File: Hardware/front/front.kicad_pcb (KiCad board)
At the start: 4 copper layers, 75 x 60 mm, 27 parts, among them J101 Conn_02x10_Odd_Even, SW101 Alps EC11E, SW102 C&K-D6R-Illuminated, SW103 B3W-9002-Y1C, SW104 B3W-9002-Y1C, SW105 B3W-9002-Y1C, SW106 B3W-9002-Y1C, SW107 B3W-9000-RHG2C, U101 XRA1203, U102 AT24CS32-SSHM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

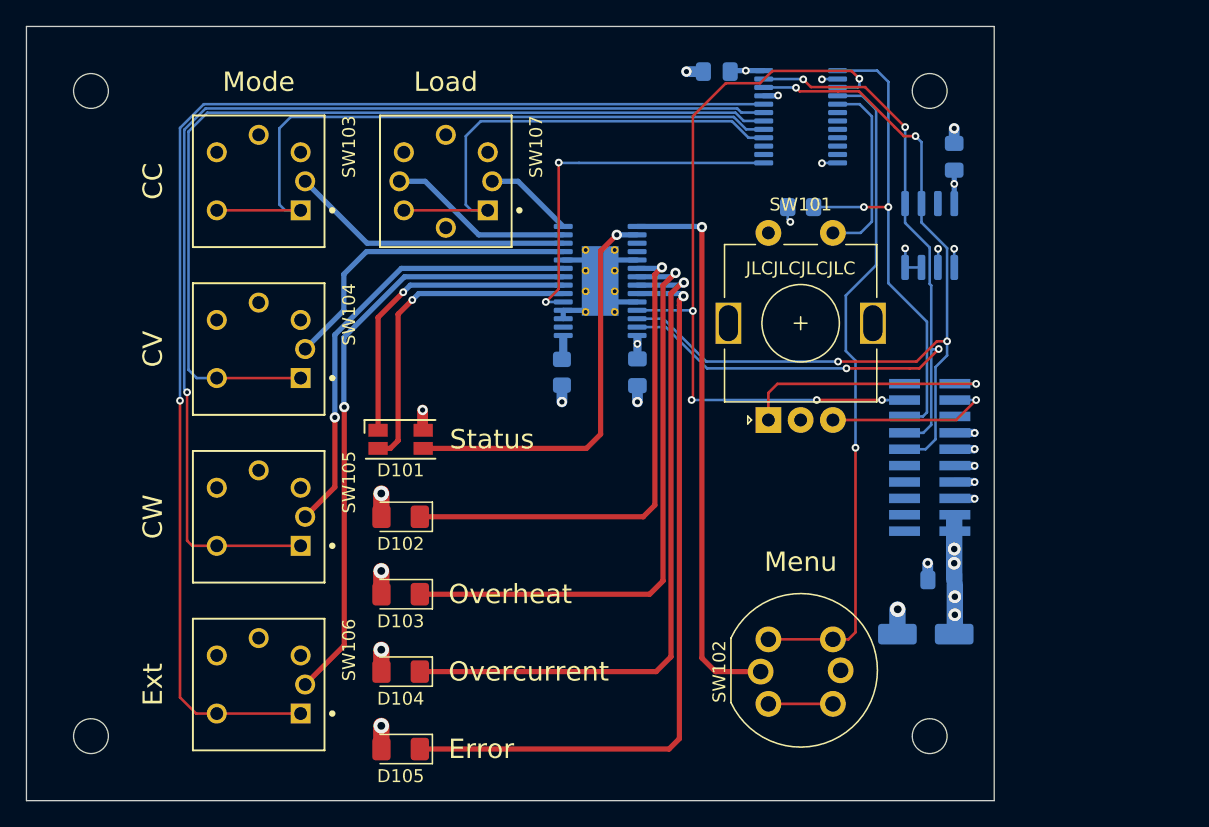
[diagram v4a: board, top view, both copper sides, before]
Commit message: Rev 2 for front panel
- Adds debouncing for all switches on the board itself, and fixes the
  incorrect RGB LED footprint.

- Fix Omron B3W-9XXX switch footprints (they had soldermask over copper)
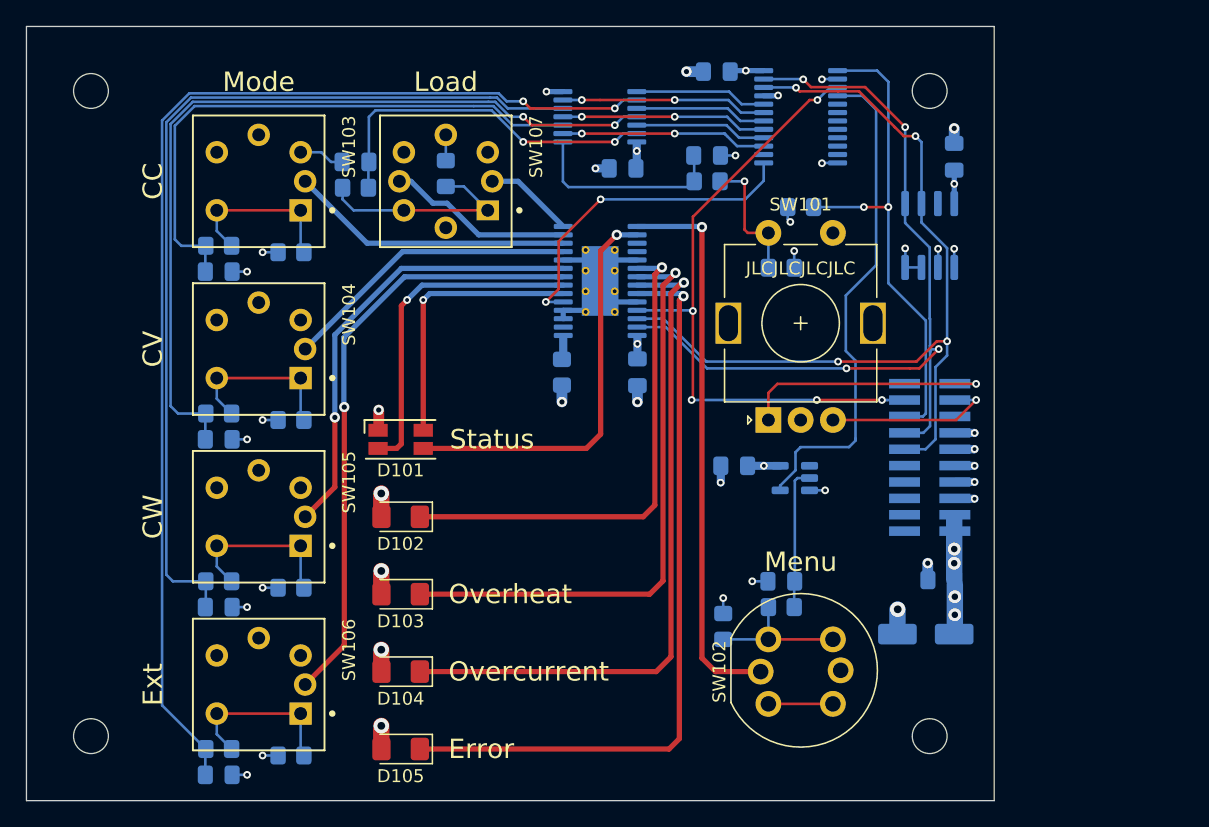
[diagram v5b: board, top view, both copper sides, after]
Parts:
- added C103: 100nF, Capacitor_SMD:C_0805_2012Metric_Pad1.18x1.45mm_HandSolder, B.Cu at (61.2, 31.0)
- added C107: 4.7µF, Capacitor_SMD:C_0805_2012Metric_Pad1.18x1.45mm_HandSolder, B.Cu at (29.9, 39.0)
- added C108: 4.7µF, Capacitor_SMD:C_0805_2012Metric_Pad1.18x1.45mm_HandSolder, B.Cu at (29.9, 52.0)
- added C109: 4.7µF, Capacitor_SMD:C_0805_2012Metric_Pad1.18x1.45mm_HandSolder, B.Cu at (29.9, 65.0)
- added C110: 4.7µF, Capacitor_SMD:C_0805_2012Metric_Pad1.18x1.45mm_HandSolder, B.Cu at (29.9, 78.0)
- added C111: 4.7µF, Capacitor_SMD:C_0805_2012Metric_Pad1.18x1.45mm_HandSolder, B.Cu at (40.5, 30.5)
- added C112: 4.7µF, Capacitor_SMD:C_0805_2012Metric_Pad1.18x1.45mm_HandSolder, B.Cu at (67.8, 30.0)
- added C113: 4.7µF, Capacitor_SMD:C_0805_2012Metric_Pad1.18x1.45mm_HandSolder, B.Cu at (73.5, 63.0)
- added C114: 100nF, Capacitor_SMD:C_0805_2012Metric_Pad1.18x1.45mm_HandSolder, B.Cu at (69.8, 54.0)
- added G***: LOGO, LOGO, B.Cu at (59.0, 71.4)
- added R103: 10k, Resistor_SMD:R_0805_2012Metric_Pad1.20x1.40mm_HandSolder, B.Cu at (35.5, 37.5)
- added R104: 10k, Resistor_SMD:R_0805_2012Metric_Pad1.20x1.40mm_HandSolder, B.Cu at (35.5, 50.5)
- added R105: 10k, Resistor_SMD:R_0805_2012Metric_Pad1.20x1.40mm_HandSolder, B.Cu at (35.5, 63.5)
- added R106: 10k, Resistor_SMD:R_0805_2012Metric_Pad1.20x1.40mm_HandSolder, B.Cu at (35.5, 76.5)
- added R107: 10k, Resistor_SMD:R_0805_2012Metric_Pad1.20x1.40mm_HandSolder, B.Cu at (47.5, 31.4)
- added R108: 1k, Resistor_SMD:R_0805_2012Metric_Pad1.20x1.40mm_HandSolder, B.Cu at (29.9, 37.0)
- added R109: 1k, Resistor_SMD:R_0805_2012Metric_Pad1.20x1.40mm_HandSolder, B.Cu at (29.9, 50.0)
- added R110: 1k, Resistor_SMD:R_0805_2012Metric_Pad1.20x1.40mm_HandSolder, B.Cu at (29.9, 63.0)
- added R111: 1k, Resistor_SMD:R_0805_2012Metric_Pad1.20x1.40mm_HandSolder, B.Cu at (29.9, 76.0)
- added R112: 1k, Resistor_SMD:R_0805_2012Metric_Pad1.20x1.40mm_HandSolder, B.Cu at (40.5, 32.5)
- added R113: 10k, Resistor_SMD:R_0805_2012Metric_Pad1.20x1.40mm_HandSolder, B.Cu at (73.5, 38.7)
- added R114: 1k, Resistor_SMD:R_0805_2012Metric_Pad1.20x1.40mm_HandSolder, B.Cu at (67.8, 32.0)
- added R115: 1k, Resistor_SMD:R_0805_2012Metric_Pad1.20x1.40mm_HandSolder, B.Cu at (73.5, 65.0)
- added R116: 10k, Resistor_SMD:R_0805_2012Metric_Pad1.20x1.40mm_HandSolder, B.Cu at (69.0, 66.5)
- added U104: 74LV14, Package_SO:TSSOP-14_4.4x5mm_P0.65mm, B.Cu at (59.4, 27.0)
- added U105: 74LVC1G14GV, Package_TO_SOT_SMD:SOT-23-5, B.Cu at (74.5, 55.0)
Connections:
- D101 pad 1: /LED_STATUS_R -> +3V3
- D101 pad 2: /LED_STATUS_G -> /LED_STATUS_B
- D101 pad 3: /LED_STATUS_B -> /LED_STATUS_R
- D101 pad 4: +3V3 -> /LED_STATUS_G
- SW101 pad S1: /SW_ENCODER -> GND
- SW101 pad S2: GND -> Net-(SW101-PadS2)
- SW102 pad 1: /SW_MENU -> Net-(R115-Pad2)
- SW102 pad 2: /SW_MENU -> Net-(R115-Pad2)
- SW103 pad 1: /SW_MODE_CC -> Net-(R103-Pad1)
- SW103 pad 2: /SW_MODE_CC -> Net-(R103-Pad1)
- SW104 pad 1: /SW_MODE_CV -> Net-(R104-Pad1)
- SW104 pad 2: /SW_MODE_CV -> Net-(R104-Pad1)
- SW105 pad 1: /SW_MODE_CW -> Net-(R105-Pad1)
- SW105 pad 2: /SW_MODE_CW -> Net-(R105-Pad1)
- SW106 pad 1: /SW_MODE_EXT -> Net-(R106-Pad1)
- SW106 pad 2: /SW_MODE_EXT -> Net-(R106-Pad1)
- SW107 pad 1: /SW_ENABLE -> Net-(R107-Pad1)
- SW107 pad 2: /SW_ENABLE -> Net-(R107-Pad1)
- U101 pad 15: unconnected-(U101-Pad15) -> /SW_ENCODER
- U101 pad 5: /SW_ENCODER -> unconnected-(U101-Pad5)
- U103 pad 16: /LED_STATUS_B -> /LED_STATUS_R
- U103 pad 7: /LED_STATUS_R -> /LED_STATUS_B
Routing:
- net Net-(C110-Pad1): track 0.00 -> 90.5 mm, vias 0 -> 2
- net /SW_MODE_EXT: track 100.0 -> 10.2 mm, vias 1 -> 0
- net Net-(C109-Pad1): track 0.00 -> 72.2 mm
- net /SW_MODE_CW: track 86.6 -> 16.0 mm, vias 1 -> 2
- net Net-(C108-Pad1): track 0.00 -> 64.7 mm, vias 0 -> 2
- net /SW_MODE_CV: track 72.9 -> 10.2 mm
- net Net-(C107-Pad1): track 0.00 -> 44.7 mm
- net /SW_MODE_CC: track 52.5 -> 16.0 mm, vias 0 -> 2
- net Net-(C111-Pad1): track 0.00 -> 27.8 mm, vias 0 -> 2
- net /SW_ENABLE: track 37.8 -> 10.2 mm
- net Net-(R107-Pad1): track 0.00 -> 16.5 mm
- net Net-(U104-Pad1): track 0.00 -> 15.6 mm
- net GND: track 36.6 -> 52.0 mm, vias 17 -> 27
- net +3V3: track 24.5 -> 37.9 mm, vias 13 -> 21
- net /SW_MENU: track 52.2 -> 38.8 mm, vias 1 -> 0
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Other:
- board text added: "Rev 2"
- board text removed: "Rev 1"

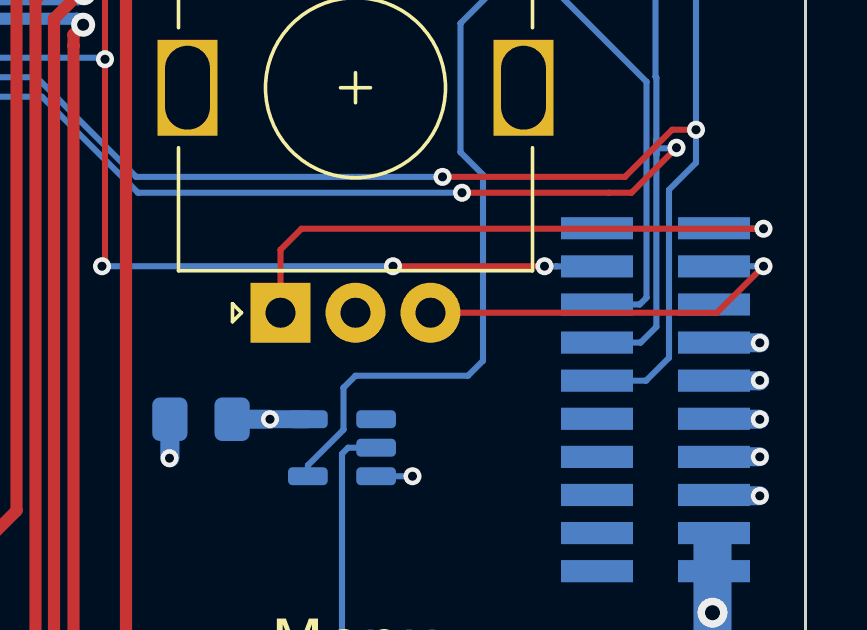
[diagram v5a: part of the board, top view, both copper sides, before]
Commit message: More tweaks to rev 2 front panel
- Added on-board pull ups for encoder lines, to reduce noise carried on
  the lines

- Cleaned up a few traces

- Actually fixed the footprint of the RGB LED so that not only does the
  common terminal match up, as do all three of the color terminals also
  :D
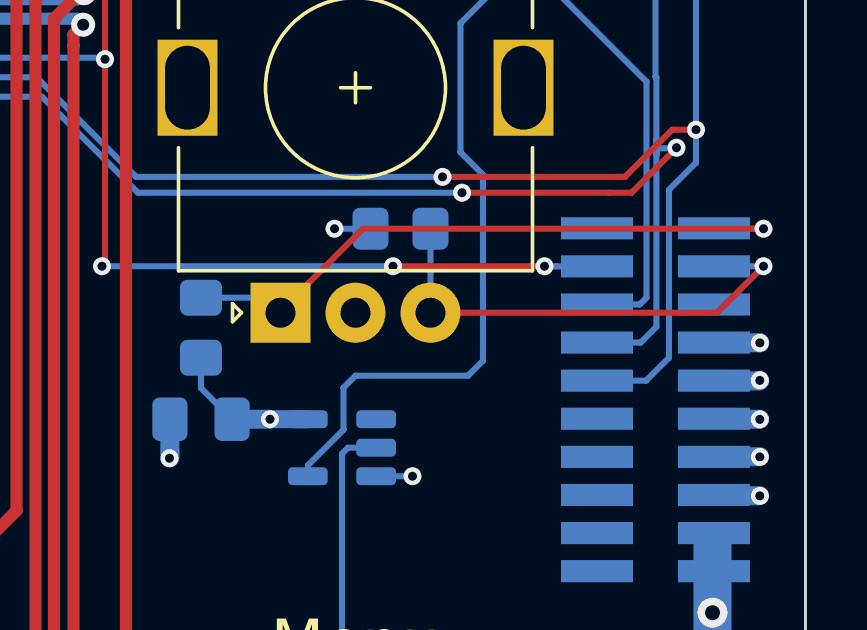
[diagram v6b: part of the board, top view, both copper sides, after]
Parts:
- added R117: 10k, Resistor_SMD:R_0805_2012Metric_Pad1.20x1.40mm_HandSolder, B.Cu at (69.8, 51.0)
- added R118: 10k, Resistor_SMD:R_0805_2012Metric_Pad1.20x1.40mm_HandSolder, B.Cu at (76.5, 47.7)
- moved G*** 6.65 mm to (52.5, 70.0)
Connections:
- D101 pad 2: /LED_STATUS_B -> /LED_STATUS_R
- D101 pad 3: /LED_STATUS_R -> /LED_STATUS_G
- D101 pad 4: /LED_STATUS_G -> /LED_STATUS_B
- U103 pad 16: /LED_STATUS_R -> /LED_STATUS_G
- U103 pad 6: /LED_STATUS_G -> /LED_STATUS_B
- U103 pad 7: /LED_STATUS_B -> /LED_STATUS_R
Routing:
- net /LED_STATUS_G: track 21.2 -> 31.7 mm
- net /LED_STATUS_R: track 31.7 -> 25.9 mm
- net /LED_STATUS_B: track 25.9 -> 21.2 mm
- net +3V3: track 37.9 -> 41.6 mm, vias 21 -> 22
- net /ENCODER_B: track 13.4 -> 16.2 mm
- net /ENCODER_A: track 20.1 -> 21.8 mm

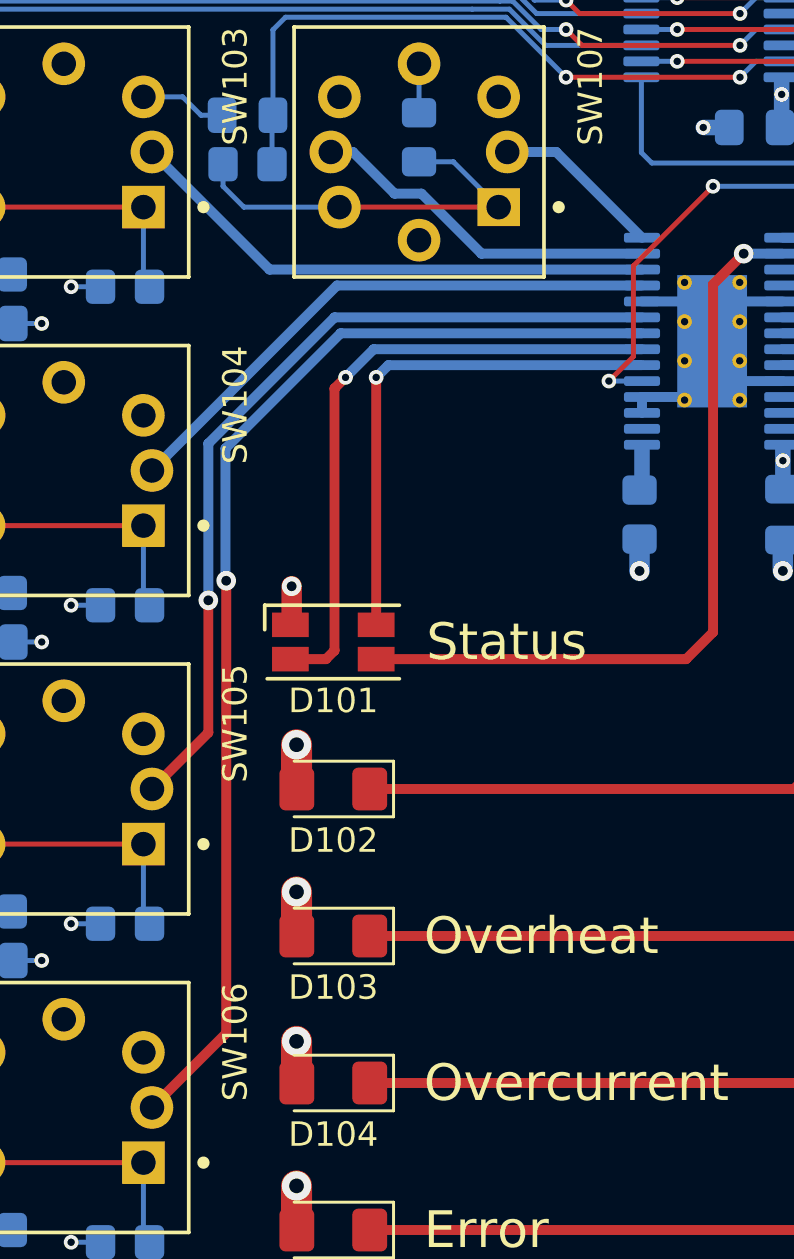
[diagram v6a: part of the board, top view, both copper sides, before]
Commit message: More work on rev2 driver board
- Tweaked the board layout for the load driver some more, primarily
  relating to power and friends

- Fixed footprint of fan connector on driver board (to properly have the
  mechanical mounting hole)

- Manufacturability/solderability tweaks for a few other footprints
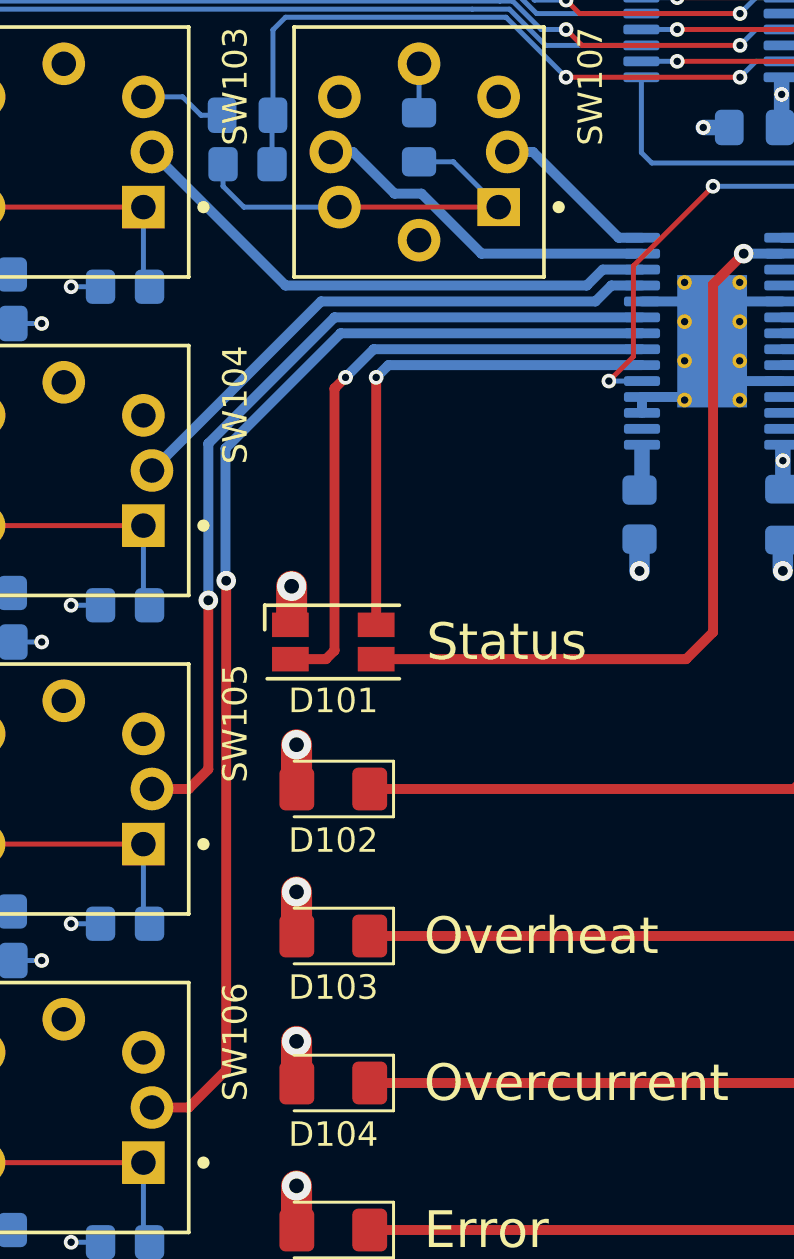
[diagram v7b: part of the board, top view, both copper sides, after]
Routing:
- net /LED_MODE_EXT: track 47.1 -> 48.0 mm
- net /LED_MODE_CW: track 34.9 -> 35.8 mm
- net /LED_MODE_CC: track 22.0 -> 22.5 mm
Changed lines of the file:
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@@
   (segment (start 42.5 75.8125) (end 42.5 74.2) (width 1.27) (layer "F.Cu") (net 1))
   (segment (start 42.5 69.9125) (end 42.5 68.3) (width 1.27) (layer "F.Cu") (net 1))
-  (segment (start 42.3 51.275) (end 42.3 49.725) (width 0.8382) (layer "F.Cu") (net 1))
+  (segment (start 42.3 51.1) (end 42.3 49.725) (width 1.27) (layer "F.Cu") (net 1))
   (segment (start 42.5 57.80625) (end 42.5 56.19375) (width 1.27) (layer "F.Cu") (net 1))
   (segment (start 42.5 63.8125) (end 42.5 62.2) (width 1.27) (layer "F.Cu") (net 1))
@@
   (via (at 42.5 74.2) (size 1.2) (drill 0.6) (layers "F.Cu" "B.Cu") (net 1))
   (via (at 62.35 44.6) (size 0.6) (drill 0.3) (layers "F.Cu" "B.Cu") (net 1))
-  (via (at 42.3 49.725) (size 0.8) (drill 0.4) (layers "F.Cu" "B.Cu") (net 1))
+  (via (at 42.3 49.725) (size 1.2) (drill 0.6) (layers "F.Cu" "B.Cu") (net 1))
   (segment (start 73.4125 54.05) (end 72.15 54.05) (width 0.6) (layer "B.Cu") (net 1))
   (segment (start 86.905 31.3425) (end 86.9 31.3375) (width 0.4064) (layer "B.Cu") (net 1))
@@
   (segment (start 69.3 27) (end 70.275 27.975) (width 0.2032) (layer "B.Cu") (net 32))
   (segment (start 56.575 27) (end 58.0375 27) (width 0.2032) (layer "B.Cu") (net 32))
-  (segment (start 41.4 36.8) (end 36.6 32) (width 0.4064) (layer "B.Cu") (net 33))
-  (segment (start 56.6 36.8) (end 41.4 36.8) (width 0.4064) (layer "B.Cu") (net 33))
+  (segment (start 56.6 36.8) (end 54.998169 36.8) (width 0.4064) (layer "B.Cu") (net 33))
+  (segment (start 54.348169 37.45) (end 42.05 37.45) (width 0.4064) (layer "B.Cu") (net 33))
+  (segment (start 42.05 37.45) (end 36.6 32) (width 0.4064) (layer "B.Cu") (net 33))
+  (segment (start 54.998169 36.8) (end 54.348169 37.45) (width 0.4064) (layer "B.Cu") (net 33))
   (segment (start 62.3 26.35) (end 69.35 26.35) (width 0.2032) (layer "B.Cu") (net 34))
   (segment (start 70.325 27.325) (end 72.1375 27.325) (width 0.2032) (layer "B.Cu") (net 34))
   (segment (start 69.35 26.35) (end 70.325 27.325) (width 0.2032) (layer "B.Cu") (net 34))
-  (segment (start 44.15 37.45) (end 36.6 45) (width 0.4064) (layer "B.Cu") (net 35))
-  (segment (start 56.6 37.45) (end 44.15 37.45) (width 0.4064) (layer "B.Cu") (net 35))
+  (segment (start 55.35 37.45) (end 54.7 38.1) (width 0.4064) (layer "B.Cu") (net 35))
+  (segment (start 43.5 38.1) (end 36.6 45) (width 0.4064) (layer "B.Cu") (net 35))
+  (segment (start 56.6 37.45) (end 55.35 37.45) (width 0.4064) (layer "B.Cu") (net 35))
+  (segment (start 54.7 38.1) (end 43.5 38.1) (width 0.4064) (layer "B.Cu") (net 35))
   (segment (start 65.2375 25.7) (end 59.4375 25.7) (width 0.2032) (layer "F.Cu") (net 36))
   (segment (start 59.4375 25.7) (end 58.0375 25.7) (width 0.2032) (layer "F.Cu") (net 36))
@@
   (segment (start 58.0375 25.7) (end 56.575 25.7) (width 0.2032) (layer "B.Cu") (net 36))
   (segment (start 70.375 26.675) (end 69.4 25.7) (width 0.2032) (layer "B.Cu") (net 36))
-  (segment (start 38.9 50.300011) (end 38.9 55.7) (width 0.4064) (layer "F.Cu") (net 37))
-  (segment (start 38.9 55.7) (end 36.6 58) (width 0.4064) (layer "F.Cu") (net 37))
+  (segment (start 38.9 50.300011) (end 38.9 57.2) (width 0.4064) (layer "F.Cu") (net 37))
+  (segment (start 38.1 58) (end 36.6 58) (width 0.4064) (layer "F.Cu") (net 37))
+  (segment (start 38.9 57.2) (end 38.1 58) (width 0.4064) (layer "F.Cu") (net 37))
   (via (at 38.9 50.3) (size 0.8) (drill 0.4) (layers "F.Cu" "B.Cu") (net 37))
   (segment (start 38.9 50.299989) (end 38.9 43.9) (width 0.4064) (layer "B.Cu") (net 37))
@@
   (segment (start 70.425 26.025) (end 72.1375 26.025) (width 0.2032) (layer "B.Cu") (net 38))
   (segment (start 39.6297 49.5) (end 39.629711 49.500011) (width 0.4064) (layer "F.Cu") (net 39))
-  (segment (start 39.629711 67.970289) (end 36.6 71) (width 0.4064) (layer "F.Cu") (net 39))
-  (segment (start 39.629711 49.500011) (end 39.629711 67.970289) (width 0.4064) (layer "F.Cu") (net 39))
+  (segment (start 39.629711 49.500011) (end 39.629711 69.470289) (width 0.4064) (layer "F.Cu") (net 39))
+  (segment (start 38.1 71) (end 36.6 71) (width 0.4064) (layer "F.Cu") (net 39))
+  (segment (start 39.629711 69.470289) (end 38.1 71) (width 0.4064) (layer "F.Cu") (net 39))
   (via (at 39.6297 49.5) (size 0.8) (drill 0.4) (layers "F.Cu" "B.Cu") (net 39))
   (segment (start 39.6 44.1) (end 44.3 39.4) (width 0.4064) (layer "B.Cu") (net 39))
@@
   (segment (start 69.25 27.65) (end 70.225 28.625) (width 0.2032) (layer "B.Cu") (net 40))
   (segment (start 62.3 27.65) (end 69.25 27.65) (width 0.2032) (layer "B.Cu") (net 40))
-  (segment (start 53.1 32) (end 51.1 32) (width 0.4064) (layer "B.Cu") (net 41))
-  (segment (start 56.6 35.5) (end 53.1 32) (width 0.4064) (layer "B.Cu") (net 41))
+  (segment (start 52.15 32) (end 51.1 32) (width 0.4064) (layer "B.Cu") (net 41))
+  (segment (start 55.65 35.5) (end 52.15 32) (width 0.4064) (layer "B.Cu") (net 41))
+  (segment (start 56.6 35.5) (end 55.65 35.5) (width 0.4064) (layer "B.Cu") (net 41))
   (segment (start 47.6 33.7) (end 46.5 33.7) (width 0.4064) (layer "B.Cu") (net 42))
   (segment (start 46.5 33.7) (end 44.8 32) (width 0.4064) (layer "B.Cu") (net 42))
